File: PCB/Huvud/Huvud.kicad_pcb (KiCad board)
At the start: 4 copper layers, 45 x 48 mm, 73 parts, among them J1 SwReg, J10 Conn_01x04_Male, J11 Conn_01x02, J2 Conn_01x04, J3 HeaterThermistor, J4 PartFan, J5 HeaterFan, J6 Heater, J7 Conn_01x03, J8 Conn_01x02, J9 Stepper, Q1 AO3400A, Q2 AO3400A, Q4 AON7418, U2 TMC2209-LA, U5 STM32F042C6T6, U6 SN65HVD230, Y1 8Mhz

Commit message: Diodes by the connectors should be moved to allow for JST connectors be used for the fan connectors.
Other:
- board text added: "TODO: Move D1,D2,D3 away from between the connectors"
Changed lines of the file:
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@@
   (general
     (thickness 1.6)
-    (drawings 43)
+    (drawings 44)
     (tracks 789)
     (zones 0)
@@
   )
   (setup
-    (last_trace_width 0.35)
+    (last_trace_width 0.25)
     (user_trace_width 0.3)
     (user_trace_width 0.35)
@@
     )
   )
+  (gr_text "TODO:\nMove D1,D2,D3 away from between the connectors" (at 185.42 154.051) (layer Dwgs.User)
+    (effects (font (size 1 1) (thickness 0.15)) (justify left))
+  )
   (dimension 37 (width 0.15) (layer Dwgs.User)

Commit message: Small steaks preparing for v0.4
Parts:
- R11, R13, R14, R15: value 6.8k -> 4.7k
- R20, R3: value 2.2k -> 470
- R6: value 10k -> 1k
- moved R15 9.05 mm to (216.0, 137.5), turned to 180 degrees
- moved R14 8.26 mm to (201.7, 138.3), turned to 90 degrees
- moved D3 6.70 mm to (216.0, 139.1), turned to 0 degrees
- moved D1 6.67 mm to (207.7, 139.0), turned to 0 degrees
- moved D2 6.59 mm to (199.3, 139.1), turned to 0 degrees
- moved R13 6.10 mm to (207.7, 137.4), turned to 180 degrees
- moved R12 2.75 mm to (209.2, 135.6), turned to 180 degrees
- moved R10 1.47 mm to (199.3, 137.2), turned to 180 degrees
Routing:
- net GND: track 89.0 -> 83.7 mm, vias 73 -> 91
- net Net-(D3-Pad2): track 5.48 -> 2.24 mm
- net HEATER: track 20.4 -> 17.2 mm
- net Net-(D3-Pad1): track 17.5 -> 16.0 mm
- net ST_VS: track 64.8 -> 66.1 mm, vias 16 -> 15
- net Net-(D1-Pad1): track 8.34 -> 7.42 mm
- net +3V3: track 60.1 -> 59.4 mm, vias 10 -> 11
- net Net-(D2-Pad1): track 13.5 -> 12.8 mm
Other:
- board text added: "+"
- board text added: "v0.4"
- board text removed: "TODO: Move D1,D2,D3 away from between the connectors"
- board text removed: "v0.3*"

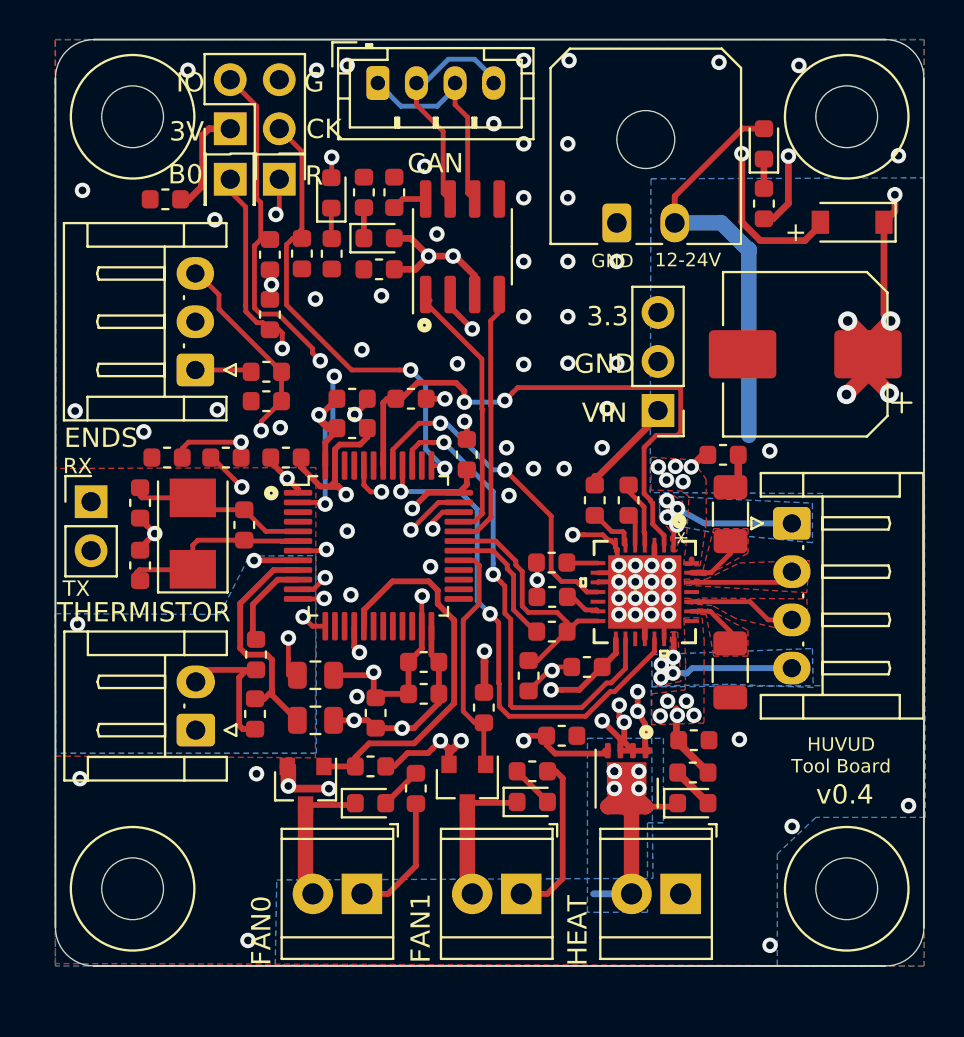
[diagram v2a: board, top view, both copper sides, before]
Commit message: Working on 0.4 Thermistor contact moved along the power contacts(can/heater) Added a micro USB connector, useful for flashing Added an on board 3.3V regulator
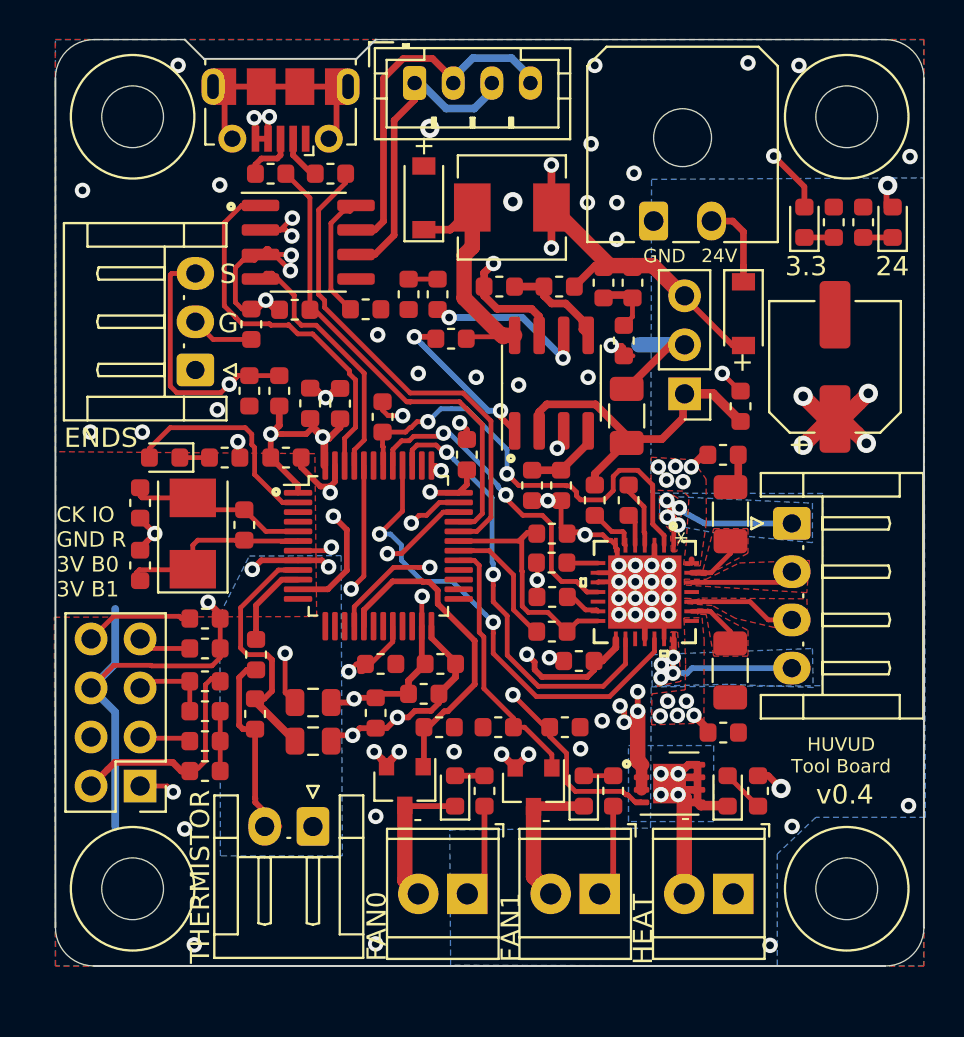
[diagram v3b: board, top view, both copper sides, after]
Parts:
- removed J11: Conn_01x02, Connector_PinHeader_2.54mm:PinHeader_1x02_P2.54mm_Vertical
- removed TP1: BOOT0, Connector_PinHeader_2.54mm:PinHeader_1x01_P2.54mm_Vertical
- removed TP2: NRST, Connector_PinHeader_2.54mm:PinHeader_1x01_P2.54mm_Vertical
- added C14: 2.2nF, Capacitor_SMD:C_0603_1608Metric, F.Cu at (201.3, 112.7)
- added C15: 15pF, Capacitor_SMD:C_0603_1608Metric, F.Cu at (207.7, 122.6)
- added C16: 10nF, Capacitor_SMD:C_0603_1608Metric, F.Cu at (209.2, 122.6)
- added C20: 10uF, Capacitor_SMD:C_1206_3216Metric, F.Cu at (212.6, 119.0)
- added C21: 0.1uF, Capacitor_SMD:C_0603_1608Metric, F.Cu at (203.5, 115.0)
- added C22: 10uF, Capacitor_SMD:C_0603_1608Metric, F.Cu at (212.9, 112.1)
- added C23: 10uF, Capacitor_SMD:C_0603_1608Metric, F.Cu at (211.4, 112.1)
- added D7: B5819W, Diode_SMD:D_SOD-123, F.Cu at (202.1, 107.7)
- added J12: USB_B_Micro, Connector_USB:USB_Micro-B_Molex-105017-0001, F.Cu at (194.7, 103.2)
- added L3: 10uH, Inductor_SMD:L_Sunlord_MWSA0518_5.4x5.2mm, F.Cu at (206.7, 108.2)
- added R25: 20, Resistor_SMD:R_0603_1608Metric, F.Cu at (194.2, 106.5)
- added R26: 20, Resistor_SMD:R_0603_1608Metric, F.Cu at (197.2, 106.5)
- added R27: 1.5k, Resistor_SMD:R_0603_1608Metric, F.Cu at (195.4, 113.5)
- added R28: 10k, Resistor_SMD:R_0603_1608Metric, F.Cu at (199.8, 131.8)
- added R29: 18k, Resistor_SMD:R_0603_1608Metric, F.Cu at (202.8, 112.7)
- added R30: 10k, Resistor_SMD:R_0603_1608Metric, F.Cu at (209.1, 112.3)
- added R31: 3.3k, Resistor_SMD:R_0603_1608Metric, F.Cu at (206.0, 112.3)
- added R32: 160k, Resistor_SMD:R_0603_1608Metric, F.Cu at (218.5, 118.5)
- added R33: 30k, Resistor_SMD:R_0603_1608Metric, F.Cu at (212.4, 115.1)
- added U1: TPS54331DR, Package_SO:SOIC-8_3.9x4.9mm_P1.27mm, F.Cu at (208.7, 117.3)
- C8: value 100uF/50V -> 100uF/35V; footprint Capacitor_SMD:CP_Elec_8x10 -> Capacitor_SMD:CP_Elec_6.3x5.8
- J2: value Conn_01x04 -> Conn_02x03; footprint Connector_PinHeader_2.54mm:PinHeader_2x02_P2.54mm_Vertical -> Connector_PinHeader_2.54mm:PinHeader_2x04_P2.54mm_Vertical
- Q4: value AON7418 -> AON7400A
- R11, R13, R14, R15: value 4.7k -> 10k
- R2: value 4.7k 1% -> 4.7k
- U5: value STM32F042C6T6 -> STM32F103C8T6
- moved J2 34.4 mm to (187.4, 138.2), turned to 180 degrees
- moved C24 29.7 mm to (190.8, 137.4), turned to 0 degrees
- moved R20 24.4 mm to (223.3, 109.0)
- moved R23 22.4 mm to (190.8, 135.8), turned to 180 degrees
- moved D8 22.0 mm to (221.8, 109.0), turned to 90 degrees
- moved R22 20.7 mm to (190.8, 131.1), turned to 0 degrees
- moved R21 19.6 mm to (190.8, 129.5), turned to 180 degrees
- moved D5 16.2 mm to (188.7, 121.2), turned to 180 degrees
- moved C19 13.3 mm to (190.8, 134.3), turned to 180 degrees
- moved R3 11.9 mm to (191.8, 121.2), turned to 0 degrees
- moved R1 11.6 mm to (190.8, 132.8), turned to 180 degrees
- moved U6 7.99 mm to (196.1, 110.0), turned to 0 degrees
- moved J3 7.86 mm to (196.3, 140.3), turned to 180 degrees
- moved D6 7.81 mm to (226.4, 109.0)
- moved R24 7.46 mm to (208.7, 125.1), turned to 180 degrees
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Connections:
- net Net-(J10-Pad1) renamed /CANL
- net Net-(J10-Pad2) renamed /CANH
- C19 pad 2: /NRST -> NRST
- C2 pad 1: GND -> ENDSTOP
- C2 pad 2: ENDSTOP -> GND
- J2 pad 1: +3V3 -> BOOT1
- J2 pad 2: SWDIO -> +3V3
- J2 pad 3: SWCLK -> BOOT0
- J2 pad 4: GND -> +3V3
- R1 pad 2: /NRST -> NRST
- R19 pad 1: +3V3 -> ENDSTOP
- R19 pad 2: ENDSTOP -> +3V3
- R22 pad 1: GND -> SWDIO
- R22 pad 2: SWDIO -> GND
- R23 pad 2: /BOOT0 -> BOOT0
- U5 pad 12: UA1_TX -> (no net)
- U5 pad 13: UA1_RX -> (no net)
- U5 pad 20: (no net) -> BOOT1
- U5 pad 32: CANRX -> USBDM
- U5 pad 33: CANTX -> USBDP
- U5 pad 44: /BOOT0 -> BOOT0
- U5 pad 45: (no net) -> CANRX
- U5 pad 46: (no net) -> CANTX
- U5 pad 7: /NRST -> NRST
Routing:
- net GND: track 83.7 -> 123.2 mm, vias 91 -> 74
- net /NRST: track 27.6 -> 0.00 mm, vias 3 -> 0
- net USBDM: track 0.00 -> 25.7 mm
- net USBDP: track 0.00 -> 25.2 mm
- net BOOT0: track 0.00 -> 24.7 mm, vias 0 -> 1
- net NRST: track 0.00 -> 22.6 mm, vias 0 -> 1
- net /BOOT0: track 22.5 -> 0.00 mm, vias 2 -> 0
- net +3V3: track 59.4 -> 80.8 mm, vias 11 -> 13
- net BOOT1: track 0.00 -> 20.4 mm, vias 0 -> 2
- net Net-(R32-Pad1): track 0.00 -> 20.3 mm, vias 0 -> 3
- net ST_VS: track 66.1 -> 47.1 mm, vias 15 -> 16
- net UA1_RX: track 18.3 -> 0.00 mm, vias 1 -> 0
- net UA1_TX: track 14.8 -> 0.00 mm, vias 1 -> 0
- net Net-(C21-Pad1): track 0.00 -> 13.1 mm
- net Net-(J12-Pad6): track 0.00 -> 12.1 mm
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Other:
- outline, holes or cut-outs redrawn
- board text added: "-"
- board text added: "24"
- board text added: "24V"
- board text added: "CK IO GND R 3V B0 3V B1"
- board text added: "S"
- board text removed: "12-24V"
- board text removed: "3V"
- board text removed: "B0"
- board text removed: "CAN"
- board text removed: "CK"
- board text removed: "IO"
- board text removed: "R"
- board text removed: "RX"
- board text removed: "TX"
- board text removed: "VIN"

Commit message: Tweaks to allow JST XH headers to fit fan outputs. PDF schematic
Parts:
- moved J5 1.14 mm to (203.2, 143.8)
- moved J3 0.84 mm to (195.5, 140.3)
- moved J6 0.38 mm to (218.5, 143.8)
- moved J4 0.35 mm to (210.8, 143.8)
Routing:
- net GND: track 123.2 -> 128.3 mm, vias 74 -> 75
- net Net-(C21-Pad2): track 8.51 -> 9.60 mm
- net Net-(D1-Pad1): track 8.42 -> 7.36 mm
- net Net-(D2-Pad1): track 7.94 -> 7.39 mm

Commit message: Final (hopefully) tweaks to v0.4 before manufacture
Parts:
- C6, C7: value 100nf/50V -> 100nF/50V
- D1, D2, D3: value LED -> LEDGR
- D5, D6, D8: value LED -> LEDRED
- J1: value SwReg -> PinHeader_1x3_P2.54mm
- J10: value Conn_01x04_Male -> JST_PH_1x04_P2.00mm_Vertical
- J12: value USB_B_Micro -> USB_Micro-B_Molex-105017-0001
- J2: value Conn_02x03 -> PinHeader_2x4_P2.54mm
- J3: value HeaterThermistor -> JST_EH_1x2_P2.50mm_Horizontal
- J4: value PartFan -> FAN0
- J5: value HeaterFan -> FAN1
- J9: value Stepper -> JST_EH_1x4_P2.50mm_Horizontal
- Q4: value AON7400A -> RU3040M2; footprint Huvud:DFN-8-1EP_3x3mm_P0.65mm_EP1.7x2.05mm -> Huvud:LFPAK33
- R4, R7: value 0.100 -> 0.110
- moved R13 0.10 mm to (211.8, 138.4)
- moved Q4 0.08 mm to (214.9, 138.0)
- moved D1 0.08 mm to (210.3, 138.4)
- turned R15 to 90 degrees
- turned R3 to 180 degrees
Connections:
- net HEATERFAN renamed FAN1
- net PARTFAN renamed FAN0
- D5 pad 2: LED0 -> +3V3
- R3 pad 1: Net-(D5-Pad1) -> LED0
- R3 pad 2: GND -> Net-(D5-Pad1)
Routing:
- net LED0: track 11.4 -> 4.26 mm
- net Net-(D3-Pad1): track 17.6 -> 11.1 mm, vias 4 -> 3
- net ST_VS: track 47.4 -> 50.8 mm, vias 16 -> 15
- net Net-(J9-Pad1): track 9.69 -> 11.2 mm
- net +3V3: track 80.8 -> 82.3 mm, vias 13 -> 14
- net Net-(J9-Pad4): track 10.6 -> 12.1 mm
- net GND: track 128.3 -> 127.1 mm
- net Net-(D3-Pad2): track 2.23 -> 1.64 mm
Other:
- board text added: "- +"
- board text added: "CK IO GND R 3.3 B0 3.3 B1"
- board text added: "ENDSTOP"
- board text removed: "CK IO GND R 3V B0 3V B1"
- board text removed: "ENDS"

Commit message: Update to v0.41
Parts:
- removed Q4: RU3040M2, Huvud:LFPAK33
- added C25: 4.7uF, Capacitor_SMD:C_0603_1608Metric, F.Cu at (194.2, 137.6)
- added Q3: AO3400A, Package_TO_SOT_SMD:SOT-23, F.Cu at (215.3, 138.2)
- C3, C6, C7, C9: value 100nF/50V -> 0.1uF
- J10: value JST_PH_1x04_P2.00mm_Vertical -> JST_PH
- J7: value Conn_01x03 -> JST_EH_1x3_P2.50mm_Horizontal
- moved R12 2.41 mm to (211.8, 135.3), turned to 90 degrees
- moved R10 1.92 mm to (204.8, 135.0), turned to 90 degrees
- moved R8 0.38 mm to (206.3, 135.0), turned to 90 degrees
- moved J1 0.11 mm to (215.7, 117.8)
- moved J3 0.08 mm to (195.5, 140.3)
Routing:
- net Net-(D3-Pad1): track 11.1 -> 7.38 mm, vias 3 -> 0
- net GNDA: track 7.05 -> 9.98 mm
- net GND: track 127.1 -> 128.4 mm, vias 75 -> 71
- net HEATER: track 24.3 -> 25.2 mm
- net ST_DIR: track 24.8 -> 25.7 mm
- net ST_UART_RX: track 12.5 -> 13.2 mm
- removed copper zone on B.Cu, net Net-(D3-Pad1)
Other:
- board text added: "v0.41"
- board text removed: "v0.4"
